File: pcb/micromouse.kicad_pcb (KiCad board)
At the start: 2 copper layers, 46 x 75.9 mm, 59 parts, among them J1 PINHD_1x6_Female, J10 B2B-PH-K-S, J11 B2B-PH-K-S, J12 PINHD_1x6_Female, J13 B6B-ZR, J14 PINHD_1x5_Male, J15 PINHD_1x5_Male, J16 PINHD_1x2_Male, J2 PINHD_1x6_Female, J3 PINHD_1x4_Female, J4 PINHD_1x6_Female, J5 PINHD_1x4_Female, J6 PINHD_1x5_Female, J7 PINHD_1x5_Female, J8 PINHD_1x2_Female, J9 B6B-ZR, M1 Left, M2 Right, SW1 SW_DIP_x04, U1 STM32F411RETx, U2 ICM-42688-P, U3 L293DD, U4 AZ1117-3.3, Y1 32.768 kHz 7 pF, Y2 25 MHz 10 pF

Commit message: Add files via upload
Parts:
- moved J16 2.65 mm to (127.0, 75.8), turned to 0 degrees
- moved J8 0.25 mm to (127.0, 95.8)
- moved NT1 0.25 mm to (136.2, 104.8)
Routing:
- net /Breakout Board/+3.3V: track 69.5 -> 71.1 mm
- net Net-(U3-PC14): track 11.6 -> 12.2 mm
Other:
- board size 46 x 75.9 mm -> 46 x 76 mm

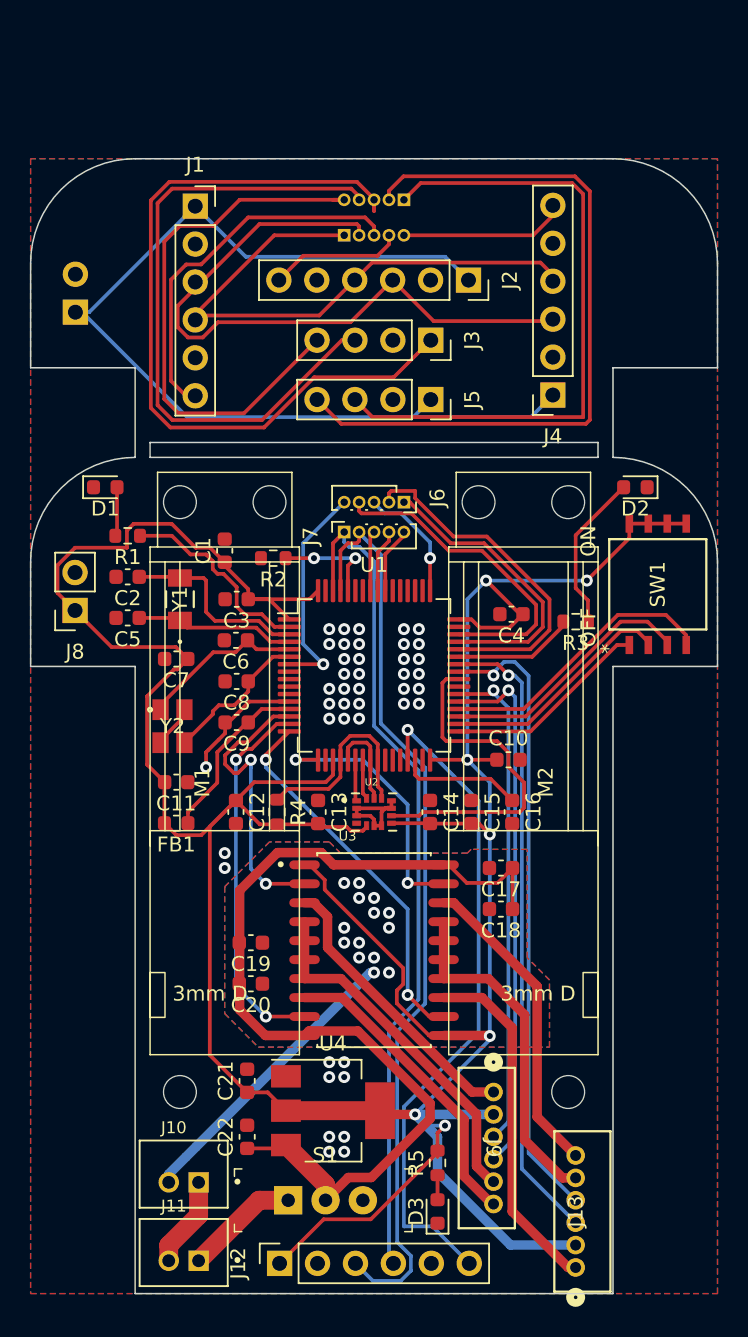
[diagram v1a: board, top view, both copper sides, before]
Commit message: Fixed folder structure
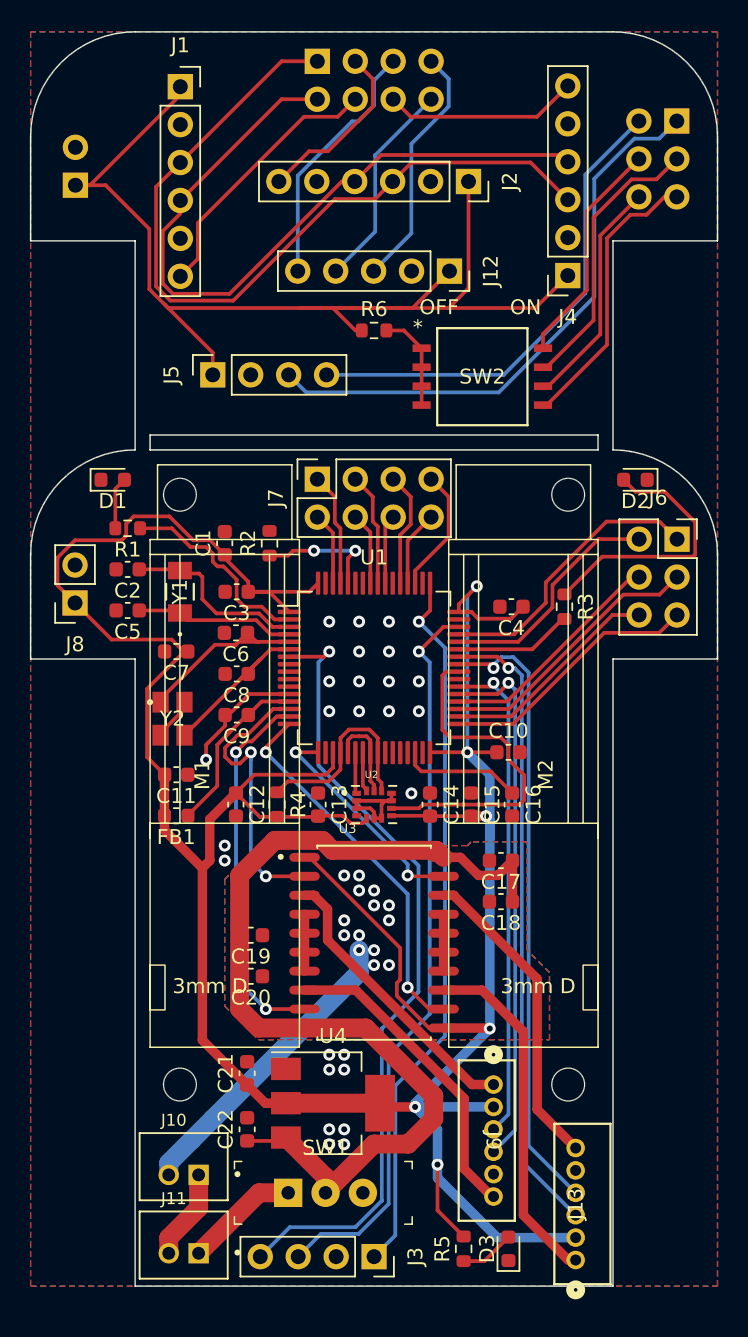
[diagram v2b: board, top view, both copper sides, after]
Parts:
- removed the SW1 at (166.0, 94.0)
- added R6: 10k, Resistor_SMD:R_0603_1608Metric, F.Cu at (147.0, 77.0)
- added SW2: SW_DIP_x04, 218-4LPST:218-4LPST, F.Cu at (154.2, 80.1)
- J12: value PINHD_1x6_Female -> PINHD_1x5_Female; footprint Connector_PinSocket_2.54mm:PinSocket_1x06_P2.54mm_Vertical -> Connector_PinSocket_2.54mm:PinSocket_1x05_P2.54mm_Vertical
- J14: value PINHD_1x5_Male -> PINHD_1x8_Male; footprint Connector_PinHeader_1.00mm:PinHeader_1x05_P1.00mm_Vertical -> Connector_PinHeader_2.54mm:PinHeader_2x04_P2.54mm_Vertical
- J15: value PINHD_1x5_Male -> PINHD_1x6_Male; footprint Connector_PinHeader_1.00mm:PinHeader_1x05_P1.00mm_Vertical -> Connector_PinHeader_2.54mm:PinHeader_2x03_P2.54mm_Vertical
- J6: value PINHD_1x5_Female -> PINHD_1x6_Female; footprint Connector_PinSocket_1.00mm:PinSocket_1x05_P1.00mm_Vertical -> Connector_PinSocket_2.54mm:PinSocket_2x03_P2.54mm_Vertical
- J7: value PINHD_1x5_Female -> PINHD_1x8_Female; footprint Connector_PinSocket_1.00mm:PinSocket_1x05_P1.00mm_Vertical -> Connector_PinSocket_2.54mm:PinSocket_2x04_P2.54mm_Vertical
- moved J12 67.4 mm to (152.1, 73.0), turned to -90 degrees
- moved J3 61.5 mm to (147.0, 139.0)
- moved J15 23.6 mm to (167.3, 63.0), turned to 180 degrees
- moved J6 18.5 mm to (167.3, 91.0), turned to 0 degrees
- moved J5 14.7 mm to (136.2, 80.0), turned to 90 degrees
- moved J14 10.9 mm to (143.2, 59.0), turned to -90 degrees
- moved J16 8.50 mm to (127.0, 67.3)
- moved J1 8.06 mm to (134.0, 60.7)
- moved J4 8.06 mm to (160.0, 73.3)
- moved J2 6.60 mm to (153.3, 67.0)
- moved R5 6.01 mm to (153.0, 138.5)
- moved D3 5.37 mm to (156.0, 138.5)
- moved J7 3.97 mm to (143.2, 87.0)
- moved NT2 1.68 mm to (135.5, 130.5)
- moved R3 1.25 mm to (159.8, 95.5), turned to -90 degrees
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- renumbered S1 to SW1
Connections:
- J12 pad 1: +3.3V -> /Breakout Board/+3.3V
- J12 pad 3: /SCL -> /Breakout Board/GPIO1
- J12 pad 4: /SDA -> /Breakout Board/GPIO2
- J12 pad 5: unconnected-(J5-Pad5) -> /Breakout Board/GPIO3
- J13 pad 5: GND1 -> GND
- J14 pad 1: /Breakout Board/USART_RX -> /Breakout Board/SCL
- J14 pad 2: /Breakout Board/USART_TX -> /Breakout Board/SDA
- J14 pad 3: /Breakout Board/SWCLK -> /Breakout Board/SHDN2
- J14 pad 4: /Breakout Board/SWDIO -> /Breakout Board/SHDN1
- J14 pad 5: /Breakout Board/NRST -> /Breakout Board/GPIO3
- J15 pad 1: /Breakout Board/SDA -> /Breakout Board/USART_RX
- J15 pad 2: /Breakout Board/SCL -> /Breakout Board/USART_TX
- J15 pad 3: /Breakout Board/SHDN1 -> /Breakout Board/DEBUG3
- J15 pad 4: /Breakout Board/SHDN2 -> /Breakout Board/DEBUG4
- J15 pad 5: /Breakout Board/SHDN3 -> /Breakout Board/DEBUG1
- J3 pad 1: /Breakout Board/SWCLK -> SWCLK
- J3 pad 3: /Breakout Board/SWDIO -> SWDIO
- J3 pad 4: /Breakout Board/NRST -> NRST
- J6 pad 3: SWCLK -> DEBUG3
- J6 pad 4: SWDIO -> DEBUG4
- J6 pad 5: NRST -> DEBUG1
- J7 pad 1: /SDA -> /SCL
- J7 pad 2: /SCL -> /SDA
- J7 pad 3: /SHDN1 -> /SHDN2
- J7 pad 4: /SHDN2 -> /SHDN1
- J7 pad 5: /SHDN3 -> GPIO3
- J9 pad 5: GND1 -> GND
- U1 pad 29: /SHDN4 -> unconnected-(U1-PB10-Pad29)
- U1 pad 51: unconnected-(U3-PC10-Pad51) -> GPIO1
- U1 pad 52: unconnected-(U3-PC11-Pad52) -> GPIO2
- U1 pad 53: unconnected-(U3-PC12-Pad53) -> GPIO3
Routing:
- net /SCL: track 61.7 -> 7.61 mm
- net /Breakout Board/SWCLK: track 52.7 -> 0.00 mm
- net /SDA: track 56.2 -> 4.86 mm
- net /SHDN4: track 44.7 -> 0.00 mm, vias 1 -> 0
- net /Breakout Board/SWDIO: track 43.5 -> 0.00 mm
- net GND1: track 63.8 -> 23.0 mm
- net SWCLK: track 8.07 -> 48.1 mm
- net NRST: track 14.8 -> 53.4 mm
- net /Breakout Board/NRST: track 36.8 -> 0.00 mm
- net +3.3V: track 239.4 -> 208.8 mm, vias 7 -> 6
- net SWDIO: track 21.8 -> 49.3 mm, vias 0 -> 1
- net /Breakout Board/DEBUG1: track 0.00 -> 18.9 mm
- net /Breakout Board/DEBUG3: track 0.00 -> 18.8 mm
- net /Breakout Board/GPIO3: track 0.00 -> 16.9 mm
- net /Breakout Board/USART_TX: track 49.2 -> 32.6 mm
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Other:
- board size 46 x 76 mm -> 46 x 84 mm

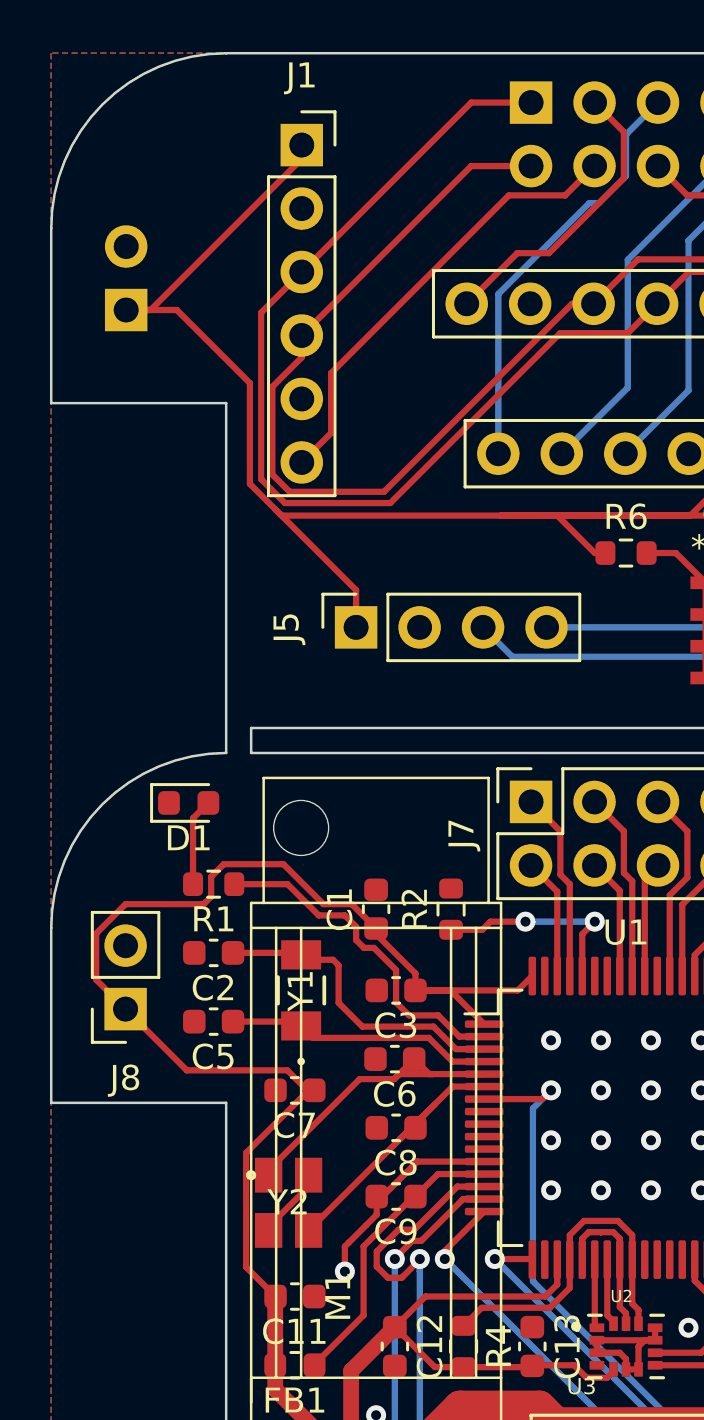
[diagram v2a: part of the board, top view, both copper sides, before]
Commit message: added "switch" (jumper)
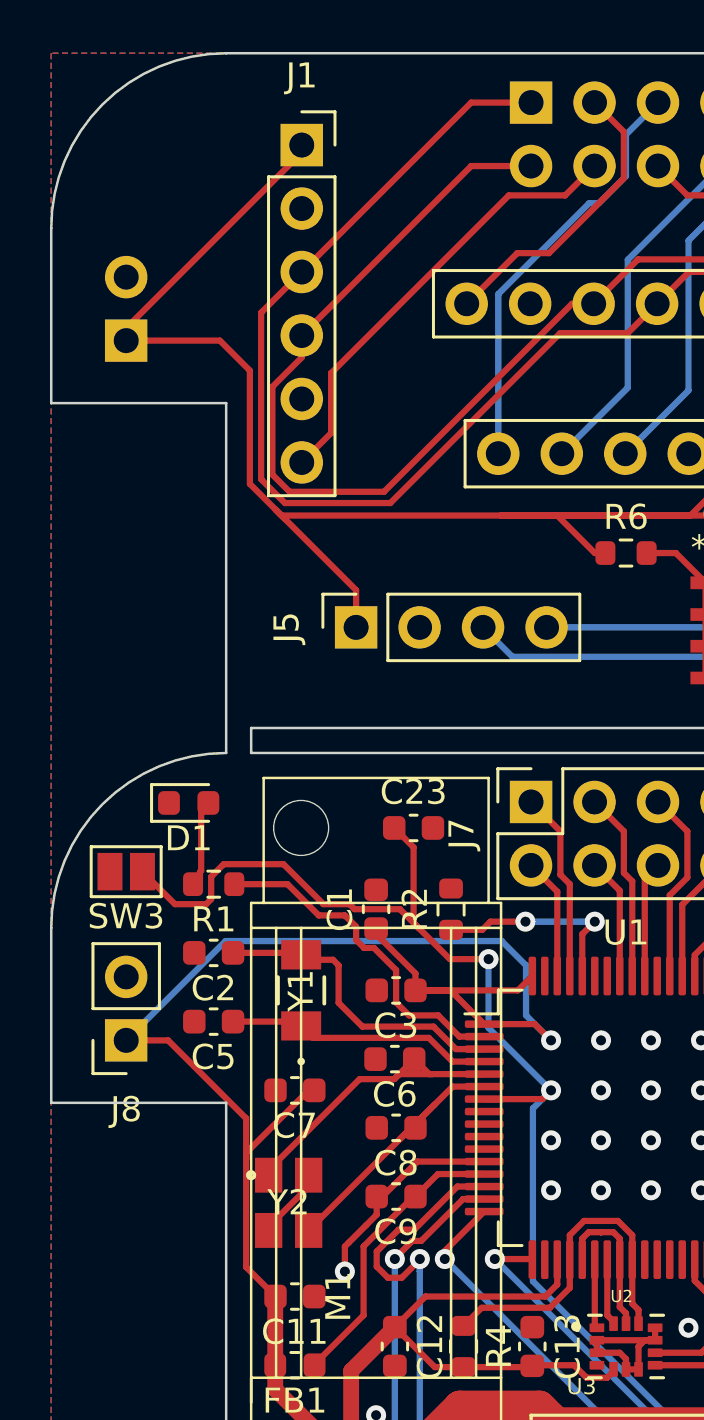
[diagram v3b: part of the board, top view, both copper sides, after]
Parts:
- added C23: 0.1 uF, Capacitor_SMD:C_0603_1608Metric, F.Cu at (138.5, 88.0)
- added SW3: Push_Button, Jumper:SolderJumper-2_P1.3mm_Open_Pad1.0x1.5mm, F.Cu at (127.0, 89.8)
- moved J8 1.25 mm to (127.0, 96.5)
- moved J16 1.22 mm to (127.0, 68.5)
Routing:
- net NRST: track 53.4 -> 81.3 mm, vias 1 -> 2
- net +3.3V: track 208.8 -> 215.0 mm, vias 6 -> 7
- net /Breakout Board/+3.3V: track 79.5 -> 80.5 mm
- net GND: vias 25 -> 24

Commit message: Update micromouse.kicad_pcb
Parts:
- moved U2 0.50 mm to (147.0, 109.2)
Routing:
- net GND1: track 23.0 -> 24.4 mm, vias 14 -> 10
- net ML2: track 19.1 -> 20.1 mm
- net +3.3V: track 215.0 -> 215.6 mm
- net /IMU/SPI_SDI: track 2.58 -> 3.16 mm
- net SPI_CS_BYPASS: track 13.6 -> 14.1 mm
- net /IMU/SPI_SD0: track 2.76 -> 3.26 mm

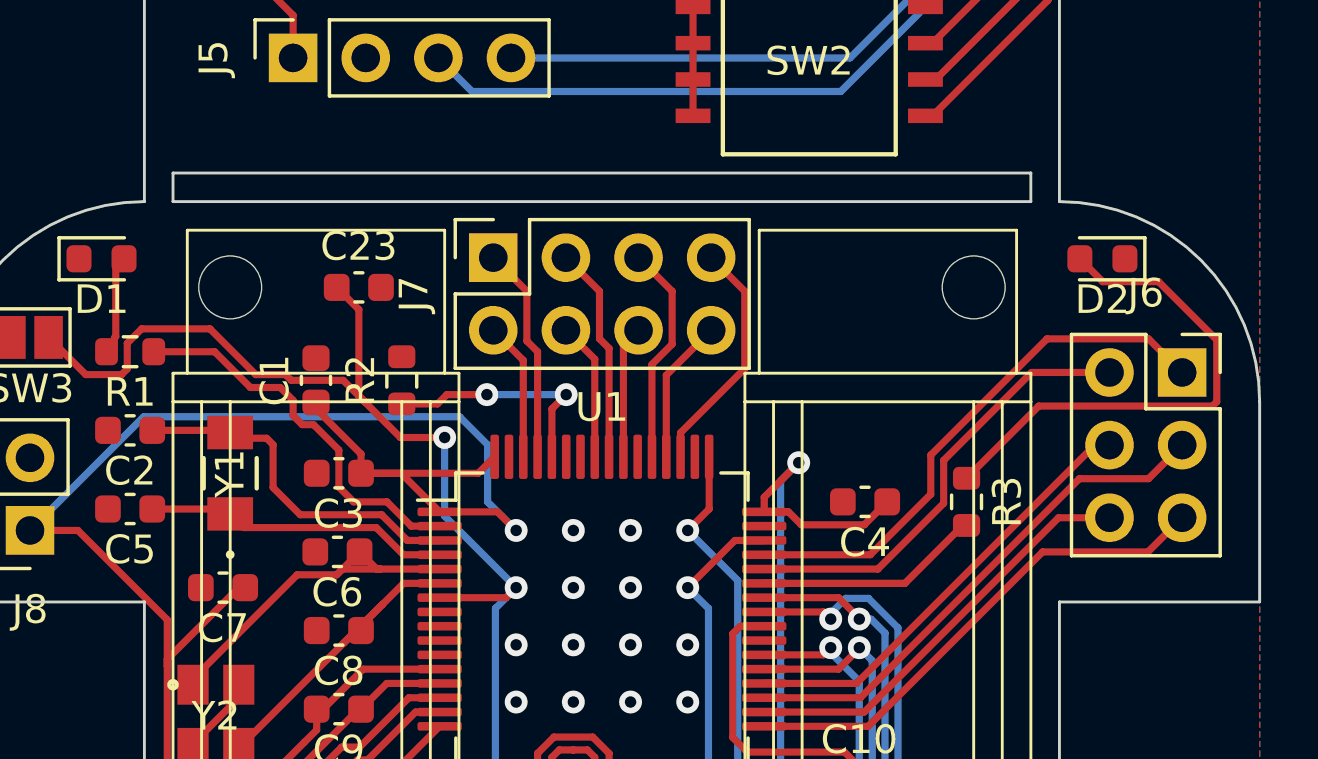
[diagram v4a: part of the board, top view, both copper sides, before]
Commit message: added reset jumper to PCB
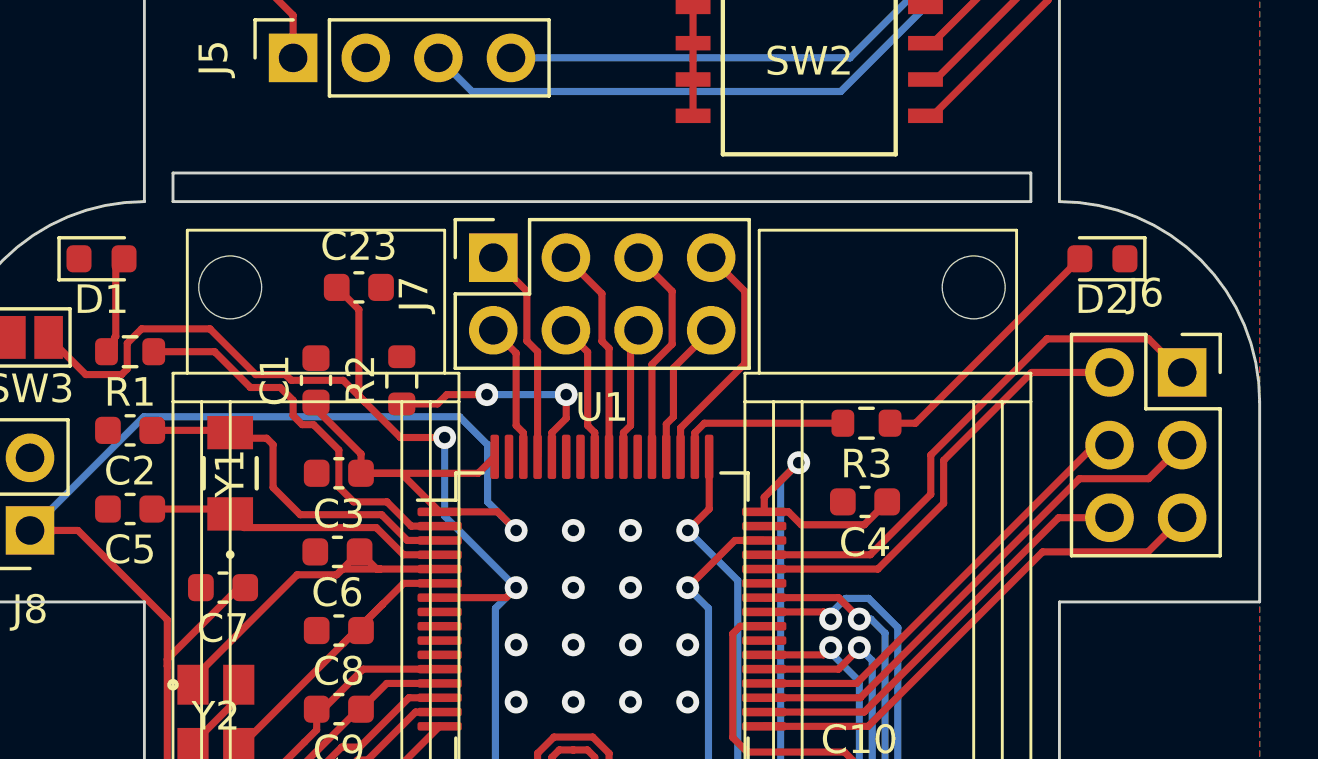
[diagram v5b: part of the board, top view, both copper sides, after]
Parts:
- moved R3 4.45 mm to (156.2, 92.8), turned to 180 degrees
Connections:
- U1 pad 43: /LED2 -> unconnected-(U1-PA10-Pad43)
- U1 pad 50: unconnected-(U1-PA15-Pad50) -> /LED2
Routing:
- net Net-(D2-A): track 18.0 -> 9.02 mm
- net /LED2: track 7.86 -> 6.16 mm
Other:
- board text added: "Mouse"
- board text added: "Potato"
- board text added: "v1"

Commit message: update board art (still need to put pictures, though)
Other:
- board text added: "2024"
- board text added: "Eric Wu Johnny You Richard Yin"
- board text added: "IEEE at UCLA"
- board text added: "mouse"
- board text added: "potato"
- board text added: "🐁"
- board text added: "🐭"
- board text removed: "Mouse"
- board text removed: "Potato"
- board text removed: "v1"
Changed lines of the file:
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@@
         (effects (font (size 1 1) (thickness 0.15)))
     )
-    (fp_circle (center -2 0) (end -1.619 0)
-      (stroke (width 0.508) (type solid)) (fill none) (layer "B.SilkS"))
     (fp_line (start -1.6221 -1.427) (end -1.6221 2.3322)
       (stroke (width 0.1524) (type solid)) (layer "F.SilkS"))
@@
         (effects (font (size 1 1) (thickness 0.15)))
     )
-    (fp_circle (center -2 0) (end -1.619 0)
-      (stroke (width 0.508) (type solid)) (fill none) (layer "B.SilkS"))
     (fp_line (start -1.6221 -1.427) (end -1.6221 2.3322)
       (stroke (width 0.1524) (type solid)) (layer "F.SilkS"))
@@
     )
   )
+  (gr_line (start 133 118) (end 149 102)
+    (stroke (width 0.15) (type default)) (layer "B.SilkS"))
+  (gr_line (start 148.5 102.5) (end 134 88)
+    (stroke (width 0.15) (type default)) (layer "B.SilkS"))
+  (gr_line (start 140.5 94.5) (end 133 102)
+    (stroke (width 0.15) (type default)) (layer "B.SilkS"))
+  (gr_line (start 148 103) (end 161 90)
+    (stroke (width 0.15) (type default)) (layer "B.SilkS"))
+  (gr_line (start 161 119) (end 141 139)
+    (stroke (width 0.15) (type default)) (layer "B.SilkS"))
   (gr_line (start 170 141) (end 165 141)
     (stroke (width 0.15) (type default)) (layer "Dwgs.User"))
@@
   (gr_line (start 132 84.999998) (end 162 85)
     (stroke (width 0.1) (type default)) (layer "Edge.Cuts"))
-  (gr_text "v1" (at 164 130 45) (layer "B.SilkS")
-    (effects (font (size 8 8) (thickness 1.6) bold) (justify left bottom mirror))
-  )
-  (gr_text "Potato" (at 164 114 45) (layer "B.SilkS")
+  (gr_text "2024" (at 139 94.5 45) (layer "B.SilkS")
+    (effects (font (size 2 2) (thickness 0.3)) (justify left bottom mirror))
+  )
+  (gr_text " 🐭" (at 154 135) (layer "B.SilkS")
+    (effects (font (size 1 1) (thickness 0.15)) (justify left bottom mirror))
+  )
+  (gr_text "potato" (at 162.5 114.5 45) (layer "B.SilkS")
     (effects (font (size 8 8) (thickness 1)) (justify left bottom mirror))
   )
-  (gr_text "Mouse" (at 164 98 45) (layer "B.SilkS")
+  (gr_text "mouse" (at 163 100 45) (layer "B.SilkS")
     (effects (font (size 8 8) (thickness 1)) (justify left bottom mirror))
   )
+  (gr_text "🐁" (at 157 132) (layer "B.SilkS")
+    (effects (font (size 1 1) (thickness 0.15)) (justify left bottom mirror))
+  )
+  (gr_text "IEEE\nat UCLA" (at 149 101 315) (layer "B.SilkS")
+    (effects (font (size 2 2) (thickness 0.3)) (justify left bottom mirror))
+  )
+  (gr_text "Eric Wu\nJohnny You\nRichard Yin" (at 147 102 45) (layer "B.SilkS")
+    (effects (font (size 2 2) (thickness 0.3)) (justify left bottom mirror))
+  )
   (dimension (type aligned) (layer "Dwgs.User")

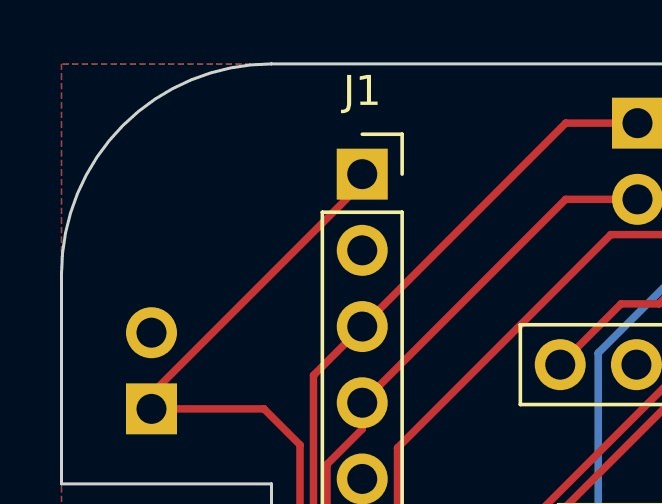
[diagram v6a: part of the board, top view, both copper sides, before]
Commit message: added board art
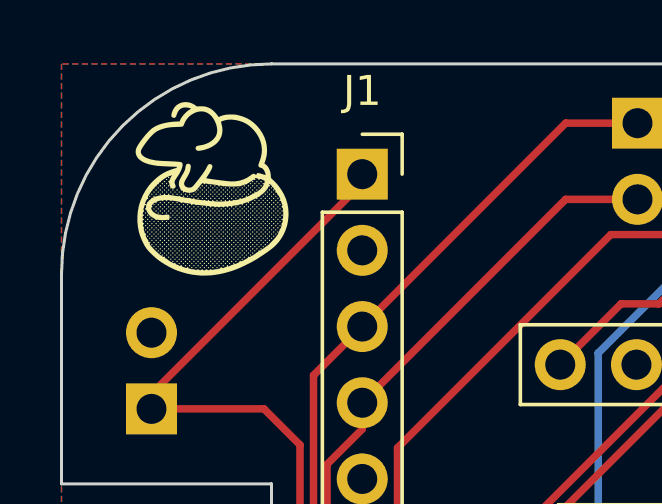
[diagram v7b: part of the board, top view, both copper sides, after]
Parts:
- added G***: LOGO, LOGO, F.Cu at (129.0, 62.0)
- added G***: LOGO, LOGO, B.Cu at (156.0, 135.7)
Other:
- board text added: "JLCJLCJLCJLC"
